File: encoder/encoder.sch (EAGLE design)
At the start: 6 parts, among them U1 AH_3761, U2 AH_3761

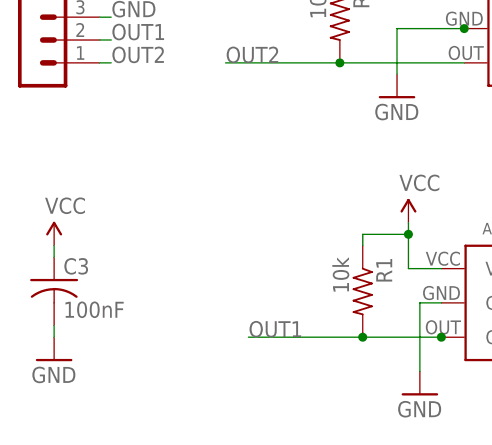
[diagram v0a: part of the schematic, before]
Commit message: Resolve stop mask errors with encoder.
Change-Id: I9fddeda359ca22c296966b7b0eabcc96fce67350
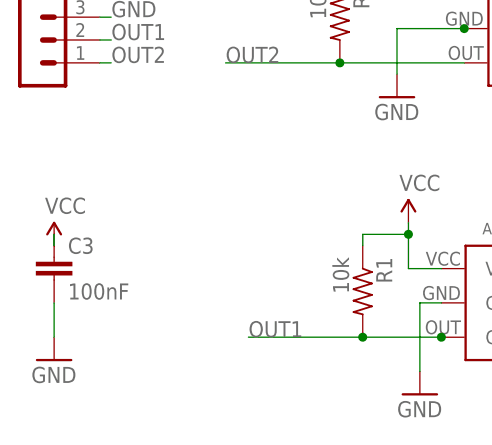
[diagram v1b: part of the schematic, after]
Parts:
- C3: device resistor:C-USC2012 -> pie:CAP0603-CAP
- R1, R2: device resistor:R-US_R3216 -> pie:R-US_R0603
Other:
- moved on the sheet: C3
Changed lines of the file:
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@@
 <layer number="144" name="Drill_legend" color="7" fill="1" visible="no" active="yes"/>
 <layer number="151" name="HeatSink" color="7" fill="1" visible="no" active="yes"/>
+<layer number="199" name="Contour" color="7" fill="1" visible="no" active="yes"/>
 <layer number="200" name="200bmp" color="1" fill="10" visible="no" active="yes"/>
 <layer number="201" name="201bmp" color="2" fill="10" visible="no" active="yes"/>
@@
 <part name="JP1" library="con-lstb" deviceset="MA04-1" device=""/>
 <part name="U2" library="custom_hall" deviceset="AH_3761" device=""/>
-<part name="R1" library="resistor" deviceset="R-US_" device="R3216" value="10k"/>
-<part name="C3" library="resistor" deviceset="C-US" device="C2012" value="100nF"/>
-<part name="R2" library="resistor" deviceset="R-US_" device="R3216" value="10k"/>
+<part name="R1" library="pie" deviceset="R-US_" device="R0603" value="10k"/>
+<part name="C3" library="pie" deviceset="CAP" device="0603-CAP" value="100nF"/>
+<part name="R2" library="pie" deviceset="R-US_" device="R0603" value="10k"/>
 <part name="U1" library="custom_hall" deviceset="AH_3761" device=""/>
 <part name="GND1" library="SparkFun-Aesthetics" deviceset="GND" device=""/>
@@
 <pinref part="C3" gate="G$1" pin="1"/>
 <pinref part="P+1" gate="1" pin="VCC"/>
-<wire x1="-36.83" y1="1.27" x2="-36.83" y2="2.54" width="0.1524" layer="91"/>
+<wire x1="-36.83" y1="3.81" x2="-36.83" y2="2.54" width="0.1524" layer="91"/>
 </segment>
 </net>
@@
 <pinref part="C3" gate="G$1" pin="2"/>
 <pinref part="GND3" gate="1" pin="GND"/>
-<wire x1="-36.83" y1="-6.35" x2="-36.83" y2="-7.62" width="0.1524" layer="91"/>
+<wire x1="-36.83" y1="-3.81" x2="-36.83" y2="-7.62" width="0.1524" layer="91"/>
 </segment>
 </net>

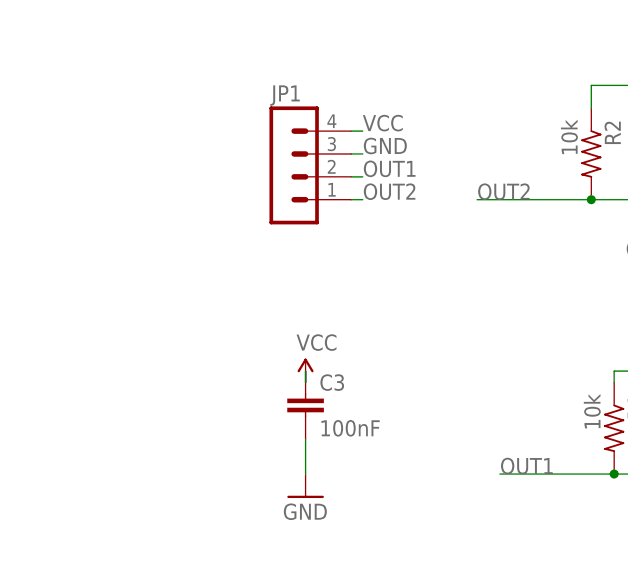
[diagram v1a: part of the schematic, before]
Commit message: Fix silk and use MTA100 on encoder
Change-Id: I97656cb59db7609cb5a5fb3d273ef94f8a7b6129
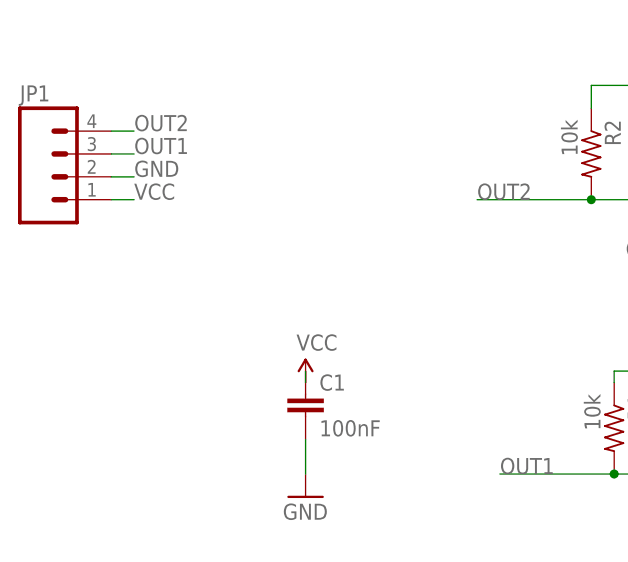
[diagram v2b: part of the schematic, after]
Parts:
- JP1: device con-lstb:MA04-1 -> pie:M04POLAR
- renumbered C3 to C1
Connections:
- net GND: now also JP1.2; no longer JP1.3
- net OUT1: now also JP1.3; no longer JP1.2
- net OUT2: now also JP1.4; no longer JP1.1
- net VCC: now also JP1.1; no longer JP1.4
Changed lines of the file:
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@@
 <layers>
 <layer number="1" name="Top" color="4" fill="1" visible="no" active="no"/>
+<layer number="2" name="Route2" color="1" fill="3" visible="no" active="no"/>
+<layer number="3" name="Route3" color="4" fill="3" visible="no" active="no"/>
+<layer number="4" name="Route4" color="1" fill="4" visible="no" active="no"/>
+<layer number="5" name="Route5" color="4" fill="4" visible="no" active="no"/>
+<layer number="6" name="Route6" color="1" fill="8" visible="no" active="no"/>
+<layer number="7" name="Route7" color="4" fill="8" visible="no" active="no"/>
+<layer number="8" name="Route8" color="1" fill="2" visible="no" active="no"/>
+<layer number="9" name="Route9" color="4" fill="2" visible="no" active="no"/>
+<layer number="10" name="Route10" color="1" fill="7" visible="no" active="no"/>
+<layer number="11" name="Route11" color="4" fill="7" visible="no" active="no"/>
+<layer number="12" name="Route12" color="1" fill="5" visible="no" active="no"/>
+<layer number="13" name="Route13" color="4" fill="5" visible="no" active="no"/>
+<layer number="14" name="Route14" color="1" fill="6" visible="no" active="no"/>
+<layer number="15" name="Route15" color="4" fill="6" visible="no" active="no"/>
 <layer number="16" name="Bottom" color="1" fill="1" visible="no" active="no"/>
 <layer number="17" name="Pads" color="2" fill="1" visible="no" active="no"/>
@@
 </classes>
 <parts>
-<part name="JP1" library="con-lstb" deviceset="MA04-1" device=""/>
 <part name="U2" library="custom_hall" deviceset="AH_3761" device=""/>
 <part name="R1" library="pie" deviceset="R-US_" device="R0603" value="10k"/>
-<part name="C3" library="pie" deviceset="CAP" device="0603-CAP" value="100nF"/>
+<part name="C1" library="pie" deviceset="CAP" device="0603-CAP" value="100nF"/>
 <part name="R2" library="pie" deviceset="R-US_" device="R0603" value="10k"/>
 <part name="U1" library="custom_hall" deviceset="AH_3761" device=""/>
@@
 <part name="P+3" library="SparkFun-Aesthetics" deviceset="VCC" device=""/>
 <part name="P+2" library="SparkFun-Aesthetics" deviceset="VCC" device=""/>
+<part name="JP1" library="pie" deviceset="M04" device="POLAR"/>
 </parts>
 <sheets>
@@
 </plain>
 <instances>
-<instance part="JP1" gate="1" x="-39.37" y="27.94"/>
 <instance part="U2" gate="G$1" x="12.7" y="26.67" rot="R180"/>
 <instance part="R1" gate="G$1" x="-2.54" y="-2.54" rot="R270"/>
-<instance part="C3" gate="G$1" x="-36.83" y="-1.27"/>
+<instance part="C1" gate="G$1" x="-36.83" y="-1.27"/>
 <instance part="R2" gate="G$1" x="-5.08" y="27.94" rot="R270"/>
 <instance part="U1" gate="G$1" x="10.16" y="-3.81" rot="R180"/>
@@
 <instance part="P+3" gate="1" x="2.54" y="5.08"/>
 <instance part="P+2" gate="1" x="2.54" y="36.83"/>
+<instance part="JP1" gate="G$1" x="-63.5" y="25.4"/>
 </instances>
 <busses>
@@
 <nets>
 <net name="OUT2" class="0">
-<segment>
-<pinref part="JP1" gate="1" pin="1"/>
-<wire x1="-31.75" y1="22.86" x2="-30.48" y2="22.86" width="0.1524" layer="91"/>
-<label x="-30.48" y="22.86" size="1.778" layer="95"/>
-</segment>
 <segment>
 <pinref part="U2" gate="G$1" pin="OUT"/>
@@
 <junction x="-5.08" y="22.86"/>
 </segment>
+<segment>
+<pinref part="JP1" gate="G$1" pin="4"/>
+<wire x1="-58.42" y1="30.48" x2="-55.88" y2="30.48" width="0.1524" layer="91"/>
+<label x="-55.88" y="30.48" size="1.778" layer="95"/>
+</segment>
 </net>
 <net name="OUT1" class="0">
-<segment>
-<pinref part="JP1" gate="1" pin="2"/>
-<wire x1="-31.75" y1="25.4" x2="-30.48" y2="25.4" width="0.1524" layer="91"/>
-<label x="-30.48" y="25.4" size="1.778" layer="95"/>
-</segment>
 <segment>
 <wire x1="6.35" y1="-7.62" x2="6.2" y2="-7.62" width="0.1524" layer="91"/>
@@
 <junction x="6.2" y="-7.62"/>
 </segment>
+<segment>
+<pinref part="JP1" gate="G$1" pin="3"/>
+<wire x1="-55.88" y1="27.94" x2="-58.42" y2="27.94" width="0.1524" layer="91"/>
+<label x="-55.88" y="27.94" size="1.778" layer="95"/>
+</segment>
 </net>
 <net name="VCC" class="0">
-<segment>
-<pinref part="JP1" gate="1" pin="4"/>
-<wire x1="-30.48" y1="30.48" x2="-31.75" y2="30.48" width="0.1524" layer="91"/>
-<label x="-30.48" y="30.48" size="1.778" layer="95"/>
-</segment>
 <segment>
 <pinref part="U1" gate="G$1" pin="VCC"/>
@@
 </segment>
 <segment>
-<pinref part="C3" gate="G$1" pin="1"/>
+<pinref part="C1" gate="G$1" pin="1"/>
 <pinref part="P+1" gate="1" pin="VCC"/>
 <wire x1="-36.83" y1="3.81" x2="-36.83" y2="2.54" width="0.1524" layer="91"/>
+</segment>
+<segment>
+<pinref part="JP1" gate="G$1" pin="1"/>
+<wire x1="-55.88" y1="22.86" x2="-58.42" y2="22.86" width="0.1524" layer="91"/>
+<label x="-55.88" y="22.86" size="1.778" layer="95"/>
 </segment>
 </net>
@@
 </segment>
 <segment>
-<pinref part="JP1" gate="1" pin="3"/>
-<wire x1="-31.75" y1="27.94" x2="-30.48" y2="27.94" width="0.1524" layer="91"/>
-<label x="-30.48" y="27.94" size="1.778" layer="95"/>
-</segment>
-<segment>
 <wire x1="6.2" y1="-3.81" x2="3.81" y2="-3.81" width="0.1524" layer="91"/>
 <pinref part="U1" gate="G$1" pin="GND"/>
@@
 </segment>
 <segment>
-<pinref part="C3" gate="G$1" pin="2"/>
+<pinref part="C1" gate="G$1" pin="2"/>
 <pinref part="GND3" gate="1" pin="GND"/>
 <wire x1="-36.83" y1="-3.81" x2="-36.83" y2="-7.62" width="0.1524" layer="91"/>
 </segment>
-</net>
+<segment>
+<pinref part="JP1" gate="G$1" pin="2"/>
+<wire x1="-55.88" y1="25.4" x2="-58.42" y2="25.4" width="0.1524" layer="91"/>
+<label x="-55.88" y="25.4" size="1.778" layer="95"/>
+</segment>
+</net>
